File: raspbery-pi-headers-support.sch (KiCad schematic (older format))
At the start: 14 parts

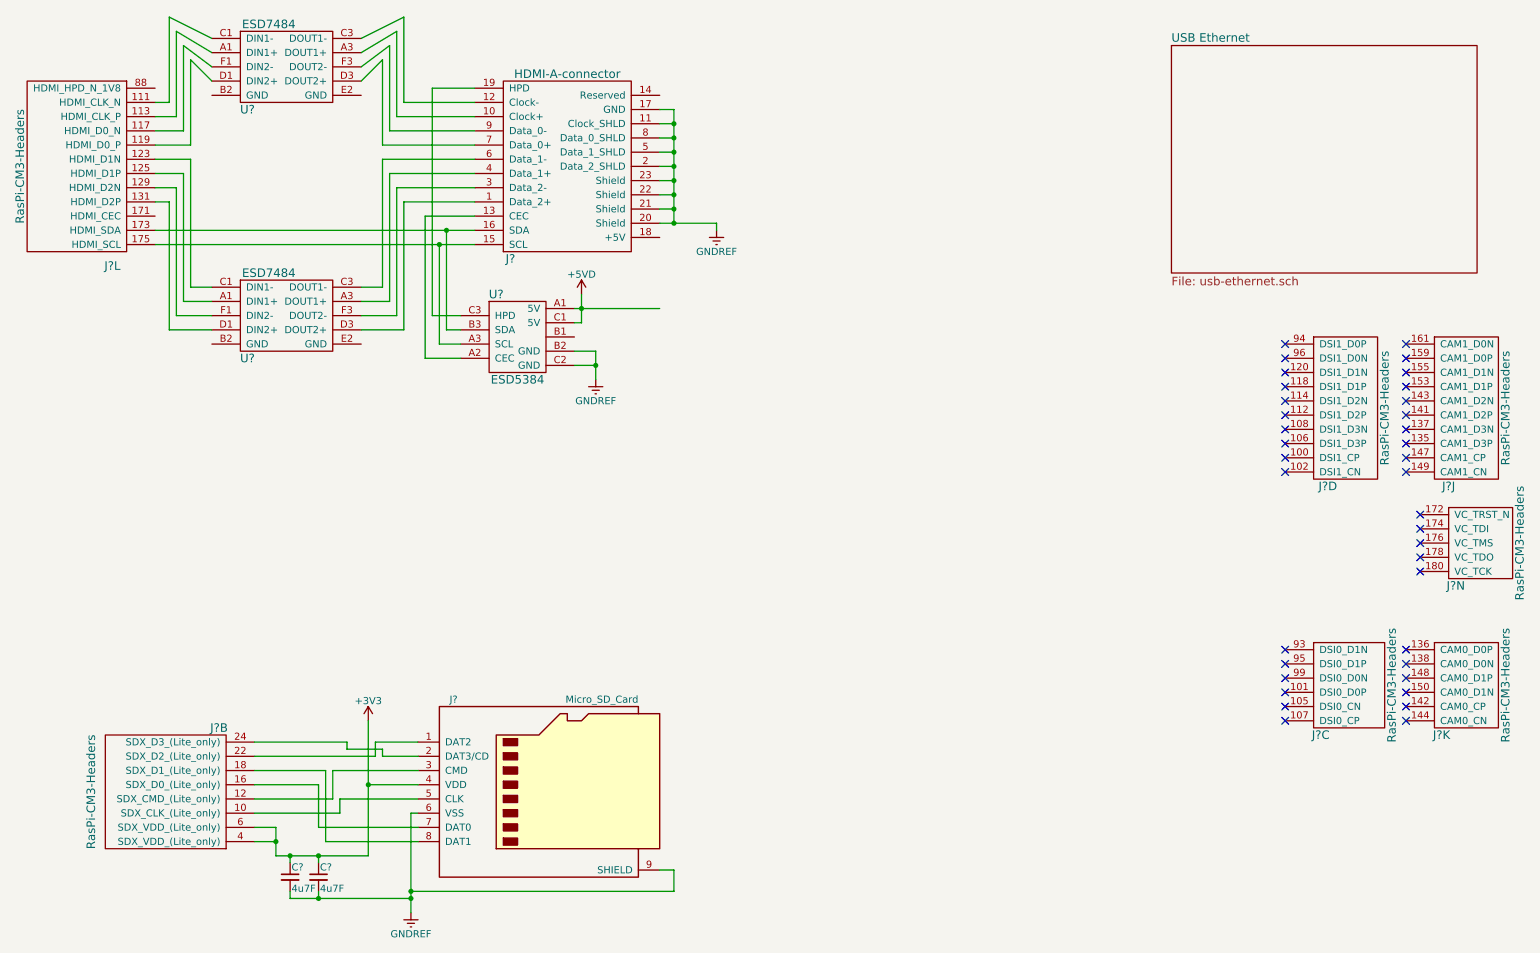
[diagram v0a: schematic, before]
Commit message: Worked on power for USB and finished ESD for hdmi
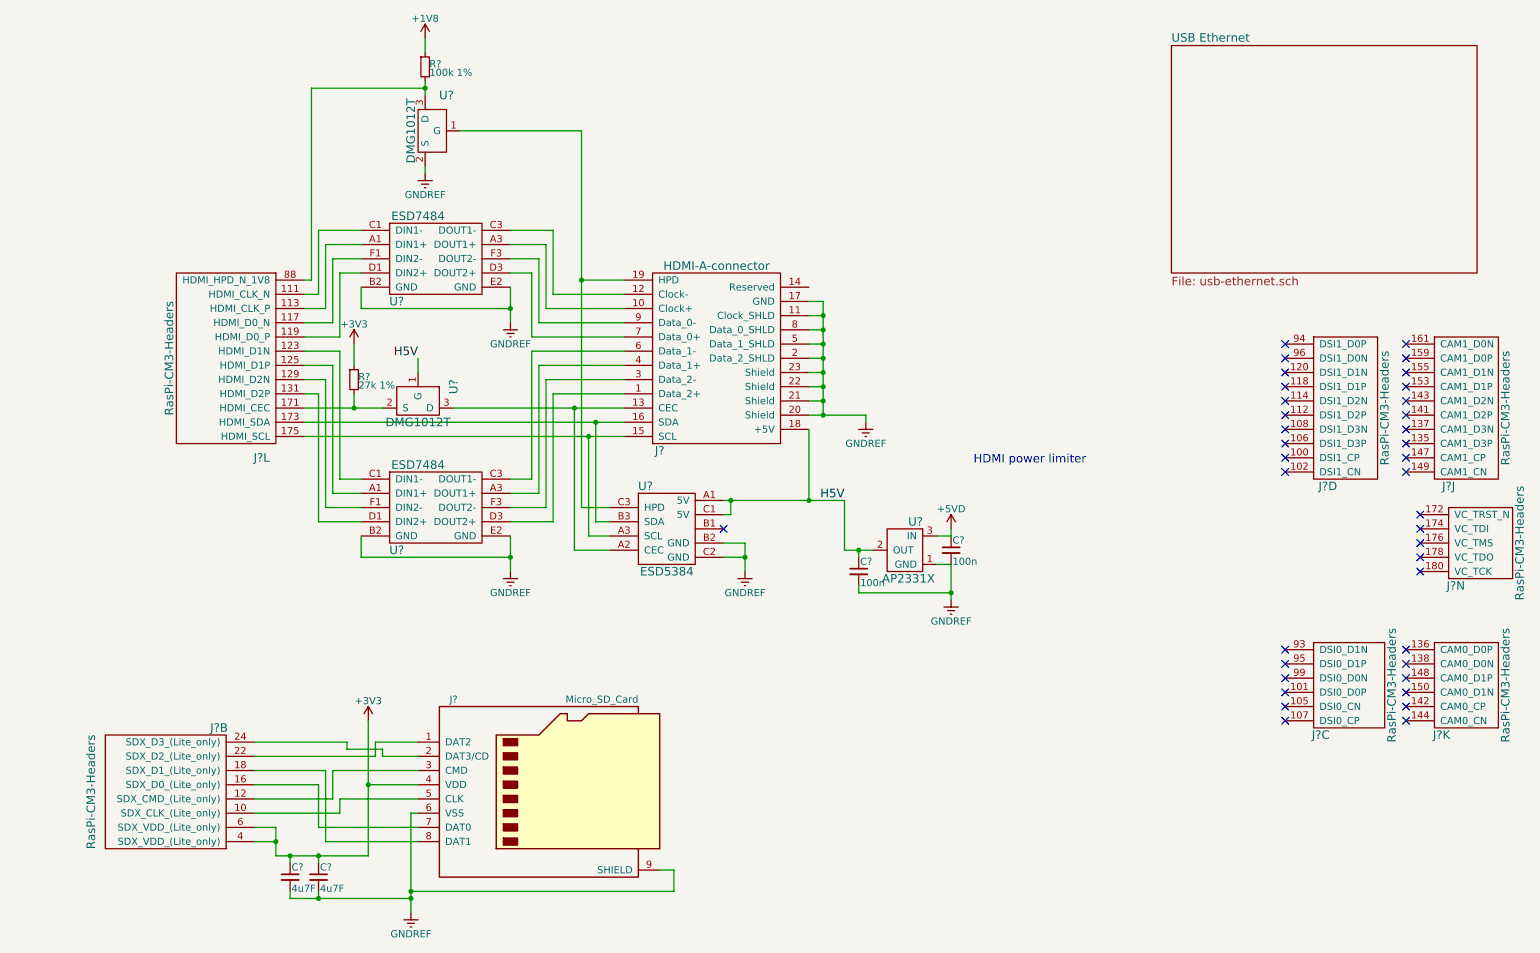
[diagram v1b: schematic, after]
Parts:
- added C? (x2): 100n, symbol C_Small
- added R?: 100k 1%, symbol R_Small
- added R?: 27k 1%, symbol R_Small
- added U? (x2): DMG1012T, symbol DMG1012T
- added U?: AP2331X, TO_SOT_Packages_SMD:SOT-23, symbol AP2331X
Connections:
- net +3V3: now also R?.1
- net +5VD: now also C?.1, U?.3 (IN); no longer U?.A1 (5V), U?.C1 (5V)
- net GNDREF: now also U?.B2 (GND), U?.B2 (GND), U?.E2 (GND), U?.E2 (GND), C?.2, C?.2, U?.1 (GND), U?.2 (S)
- net at J?.171 (HDMI_CEC): now also R?.2, U?.2 (S)
- net at J?.88 (HDMI_HPD_N_1V8): now also R?.2, U?.3 (D)
- net at J?.13 (CEC), U?.A2 (CEC): now also U?.3 (D)
- net H5V: now reaches J?.18 (+5V)
- net H5V: now also U?.A1 (5V), U?.C1 (5V), C?.1, U?.1 (G), U?.2 (OUT)
- net at J?.19 (HPD), U?.C3 (HPD): now also U?.1 (G)
- new net +1V8: R?.1
- no-connect marks 37 -> 38
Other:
- note added: "HDMI power limiter"
- moved on the sheet: J?, J?L, U?

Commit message: Started fixing DRC issues
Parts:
- C211, C212, C213, C214: renamed from C?; footprint (none) -> Capacitors_SMD:C_0603_HandSoldering
- R123, R124: renamed from R?; footprint (none) -> Capacitors_SMD:C_0603_HandSoldering
- gave numbers to parts that had none: 9
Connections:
- no-connect marks 38 -> 39
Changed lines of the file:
@@
 $EndDescr
 $Comp
-L RasPi-CM3-Headers J?
+L RasPi-CM3-Headers J1
 U 2 1 58ECDA7F
 P 1650 6000
-F 0 "J?" H 1350 5550 60  0000 C CNN
+F 0 "J1" H 1350 5550 60  0000 C CNN
 F 1 "RasPi-CM3-Headers" V 2250 6000 60  0000 C CNN
 F 2 "Sockets:Socket_SODIMM_DDR1-2_TE_1612618" H 1700 11100 60  0001 C CNN
@@
 $EndComp
 $Comp
-L RasPi-CM3-Headers J?
+L RasPi-CM3-Headers J1
 U 3 1 58ECDAC0
 P 9900 5250
-F 0 "J?" H 9700 4900 60  0000 C CNN
+F 0 "J1" H 9700 4900 60  0000 C CNN
 F 1 "RasPi-CM3-Headers" V 10200 5250 60  0000 C CNN
 F 2 "Sockets:Socket_SODIMM_DDR1-2_TE_1612618" H 9950 10350 60  0001 C CNN
@@
 $EndComp
 $Comp
-L RasPi-CM3-Headers J?
+L RasPi-CM3-Headers J1
 U 4 1 58ECDAF6
 P 9850 3300
-F 0 "J?" H 9750 2750 60  0000 C CNN
+F 0 "J1" H 9750 2750 60  0000 C CNN
 F 1 "RasPi-CM3-Headers" V 10150 3300 60  0000 C CNN
 F 2 "Sockets:Socket_SODIMM_DDR1-2_TE_1612618" H 9900 8400 60  0001 C CNN
@@
 $EndComp
 $Comp
-L RasPi-CM3-Headers J?
+L RasPi-CM3-Headers J1
 U 10 1 58ECDB2D
 P 10700 3300
-F 0 "J?" H 10600 2750 60  0000 C CNN
+F 0 "J1" H 10600 2750 60  0000 C CNN
 F 1 "RasPi-CM3-Headers" V 11000 3300 60  0000 C CNN
 F 2 "Sockets:Socket_SODIMM_DDR1-2_TE_1612618" H 10750 8400 60  0001 C CNN
@@
 $EndComp
 $Comp
-L RasPi-CM3-Headers J?
+L RasPi-CM3-Headers J1
 U 11 1 58ECDB78
 P 10700 5250
-F 0 "J?" H 10550 4900 60  0000 C CNN
+F 0 "J1" H 10550 4900 60  0000 C CNN
 F 1 "RasPi-CM3-Headers" V 11000 5250 60  0000 C CNN
 F 2 "Sockets:Socket_SODIMM_DDR1-2_TE_1612618" H 10750 10350 60  0001 C CNN
@@
 $EndComp
 $Comp
-L RasPi-CM3-Headers J?
+L RasPi-CM3-Headers J1
 U 12 1 58ECDBAE
 P 2100 2950
-F 0 "J?" H 1950 2250 60  0000 C CNN
+F 0 "J1" H 1950 2250 60  0000 C CNN
 F 1 "RasPi-CM3-Headers" V 2600 2950 60  0000 C CNN
 F 2 "Sockets:Socket_SODIMM_DDR1-2_TE_1612618" H 2150 8050 60  0001 C CNN
@@
 $EndComp
 $Comp
-L RasPi-CM3-Headers J?
+L RasPi-CM3-Headers J1
 U 14 1 58ECDBFE
 P 10700 4250
-F 0 "J?" H 10650 3950 60  0000 C CNN
+F 0 "J1" H 10650 3950 60  0000 C CNN
 F 1 "RasPi-CM3-Headers" V 11100 4250 60  0000 C CNN
 F 2 "Sockets:Socket_SODIMM_DDR1-2_TE_1612618" H 10750 9350 60  0001 C CNN
@@
 NoConn ~ 10400 4450
 $Comp
-L Micro_SD_Card J?
+L Micro_SD_Card J10
 U 1 1 591147C4
 P 4250 5950
-F 0 "J?" H 3600 6550 50  0000 C CNN
+F 0 "J10" H 3600 6550 50  0000 C CNN
 F 1 "Micro_SD_Card" H 4900 6550 50  0000 R CNN
 F 2 "" H 5400 6250 50  0001 C CNN
@@
 $EndComp
 $Comp
-L GNDREF #PWR?
+L GNDREF #PWR0152
 U 1 1 59114968
 P 3300 6850
-F 0 "#PWR?" H 3300 6600 50  0001 C CNN
+F 0 "#PWR0152" H 3300 6600 50  0001 C CNN
 F 1 "GNDREF" H 3300 6700 50  0000 C CNN
 F 2 "" H 3300 6850 50  0001 C CNN
@@
 $EndComp
 $Comp
-L +3V3 #PWR?
+L +3V3 #PWR0153
 U 1 1 59114A75
 P 3000 5500
-F 0 "#PWR?" H 3000 5350 50  0001 C CNN
+F 0 "#PWR0153" H 3000 5350 50  0001 C CNN
 F 1 "+3V3" H 3000 5640 50  0000 C CNN
 F 2 "" H 3000 5500 50  0001 C CNN
@@
 $EndComp
 $Comp
-L C_Small C?
+L C_Small C211
 U 1 1 5911519B
 P 2450 6600
-F 0 "C?" H 2460 6670 50  0000 L CNN
+F 0 "C211" H 2460 6670 50  0000 L CNN
 F 1 "4u7F" H 2460 6520 50  0000 L CNN
-F 2 "" H 2450 6600 50  0001 C CNN
+F 2 "Capacitors_SMD:C_0603_HandSoldering" H 2450 6600 50  0001 C CNN
 F 3 "" H 2450 6600 50  0001 C CNN
 	1    2450 6600
@@
 $EndComp
 $Comp
-L C_Small C?
+L C_Small C212
 U 1 1 5911521F
 P 2650 6600
-F 0 "C?" H 2660 6670 50  0000 L CNN
+F 0 "C212" H 2660 6670 50  0000 L CNN
 F 1 "4u7F" H 2660 6520 50  0000 L CNN
-F 2 "" H 2650 6600 50  0001 C CNN
+F 2 "Capacitors_SMD:C_0603_HandSoldering" H 2650 6600 50  0001 C CNN
 F 3 "" H 2650 6600 50  0001 C CNN
 	1    2650 6600
@@
 $EndComp
 $Comp
-L HDMI-A-connector J?
+L HDMI-A-connector J11
 U 1 1 5911658C
 P 5450 2950
-F 0 "J?" H 5050 3600 60  0000 C CNN
+F 0 "J11" H 5050 3600 60  0000 C CNN
 F 1 "HDMI-A-connector" H 5450 2300 60  0000 C CNN
 F 2 "" H 5450 2950 60  0001 C CNN
@@
 $EndComp
 $Comp
-L ESD5384 U?
+L ESD5384 U35
 U 1 1 591172E0
 P 5100 4150
-F 0 "U?" H 4950 4450 60  0000 C CNN
+F 0 "U35" H 4950 4450 60  0000 C CNN
 F 1 "ESD5384" H 5100 3850 60  0000 C CNN
 F 2 "" H 5100 4200 60  0001 C CNN
@@
 $EndComp
 $Comp
-L +5VD #PWR?
+L +5VD #PWR0154
 U 1 1 591176E4
 P 7100 4150
-F 0 "#PWR?" H 7100 4000 50  0001 C CNN
+F 0 "#PWR0154" H 7100 4000 50  0001 C CNN
 F 1 "+5VD" H 7100 4290 50  0000 C CNN
 F 2 "" H 7100 4150 50  0001 C CNN
@@
 Connection ~ 6200 2650
 $Comp
-L GNDREF #PWR?
+L GNDREF #PWR0155
 U 1 1 59117C76
 P 6500 3400
-F 0 "#PWR?" H 6500 3150 50  0001 C CNN
+F 0 "#PWR0155" H 6500 3150 50  0001 C CNN
 F 1 "GNDREF" H 6500 3250 50  0000 C CNN
 F 2 "" H 6500 3400 50  0001 C CNN
@@
 Connection ~ 6200 3350
 $Comp
-L GNDREF #PWR?
+L GNDREF #PWR0156
 U 1 1 59117D13
 P 5650 4450
-F 0 "#PWR?" H 5650 4200 50  0001 C CNN
+F 0 "#PWR0156" H 5650 4200 50  0001 C CNN
 F 1 "GNDREF" H 5650 4300 50  0000 C CNN
 F 2 "" H 5650 4450 50  0001 C CNN
@@
 Connection ~ 5650 4350
 $Comp
-L ESD7484 U?
+L ESD7484 U34
 U 1 1 5911871C
 P 3500 3950
-F 0 "U?" H 3200 3600 60  0000 C CNN
+F 0 "U34" H 3200 3600 60  0000 C CNN
 F 1 "ESD7484" H 3350 4200 60  0000 C CNN
 F 2 "" H 3500 3950 60  0001 C CNN
@@
 $EndComp
 $Comp
-L ESD7484 U?
+L ESD7484 U33
 U 1 1 591189BB
 P 3500 2200
-F 0 "U?" H 3200 1850 60  0000 C CNN
+F 0 "U33" H 3200 1850 60  0000 C CNN
 F 1 "ESD7484" H 3350 2450 60  0000 C CNN
 F 2 "" H 3500 2200 60  0001 C CNN
@@
 	4150 2350 4000 2350
 $Comp
-L DMG1012T U?
+L DMG1012T U31
 U 1 1 5911B6F8
 P 3150 1350
-F 0 "U?" H 2750 1600 60  0000 C CNN
+F 0 "U31" H 2750 1600 60  0000 C CNN
 F 1 "DMG1012T" V 3000 1350 60  0000 C CNN
 F 2 "" H 2750 1800 60  0001 C CNN
@@
 $EndComp
 $Comp
-L +1V8 #PWR?
+L +1V8 #PWR0157
 U 1 1 5911B770
 P 3400 700
-F 0 "#PWR?" H 3400 550 50  0001 C CNN
+F 0 "#PWR0157" H 3400 550 50  0001 C CNN
 F 1 "+1V8" H 3400 840 50  0000 C CNN
 F 2 "" H 3400 700 50  0001 C CNN
@@
 Connection ~ 4500 2400
 $Comp
-L R_Small R?
+L R_Small R124
 U 1 1 5911BA5B
 P 3400 900
-F 0 "R?" H 3430 920 50  0000 L CNN
+F 0 "R124" H 3430 920 50  0000 L CNN
 F 1 "100k 1%" H 3430 860 50  0000 L CNN
-F 2 "" H 3400 900 50  0001 C CNN
+F 2 "Capacitors_SMD:C_0603_HandSoldering" H 3400 900 50  0001 C CNN
 F 3 "" H 3400 900 50  0001 C CNN
 	1    3400 900
@@
 	3400 1000 3400 1100
 $Comp
-L GNDREF #PWR?
+L GNDREF #PWR0158
 U 1 1 5911BCE1
 P 3400 1650
-F 0 "#PWR?" H 3400 1400 50  0001 C CNN
+F 0 "#PWR0158" H 3400 1400 50  0001 C CNN
 F 1 "GNDREF" H 3400 1500 50  0000 C CNN
 F 2 "" H 3400 1650 50  0001 C CNN
@@
 Connection ~ 3400 1050
 $Comp
-L AP2331X U?
+L AP2331X U36
 U 1 1 5911C05E
 P 6700 4150
-F 0 "U?" H 6550 4200 60  0000 C CNN
+F 0 "U36" H 6550 4200 60  0000 C CNN
 F 1 "AP2331X" H 6600 3800 60  0000 C CNN
 F 2 "TO_SOT_Packages_SMD:SOT-23" H 6800 5100 60  0001 C CNN
@@
 	6100 3950 6100 3450
 $Comp
-L C_Small C?
+L C_Small C214
 U 1 1 5911FC51
 P 7100 4300
-F 0 "C?" H 7110 4370 50  0000 L CNN
+F 0 "C214" H 7110 4370 50  0000 L CNN
 F 1 "100n" H 7110 4220 50  0000 L CNN
-F 2 "" H 7100 4300 50  0001 C CNN
+F 2 "Capacitors_SMD:C_0603_HandSoldering" H 7100 4300 50  0001 C CNN
 F 3 "" H 7100 4300 50  0001 C CNN
 	1    7100 4300
@@
 	7000 4400 7100 4400
 $Comp
-L GNDREF #PWR?
+L GNDREF #PWR0159
 U 1 1 5911FE33
 P 7100 4650
-F 0 "#PWR?" H 7100 4400 50  0001 C CNN
+F 0 "#PWR0159" H 7100 4400 50  0001 C CNN
 F 1 "GNDREF" H 7100 4500 50  0000 C CNN
 F 2 "" H 7100 4650 50  0001 C CNN
@@
 	5550 4050 5550 3950
 $Comp
-L C_Small C?
+L C_Small C213
 U 1 1 59120198
 P 6450 4450
-F 0 "C?" H 6460 4520 50  0000 L CNN
+F 0 "C213" H 6460 4520 50  0000 L CNN
 F 1 "100n" H 6460 4370 50  0000 L CNN
-F 2 "" H 6450 4450 50  0001 C CNN
+F 2 "Capacitors_SMD:C_0603_HandSoldering" H 6450 4450 50  0001 C CNN
 F 3 "" H 6450 4450 50  0001 C CNN
 	1    6450 4450
@@
 H5V
 $Comp
-L GNDREF #PWR?
+L GNDREF #PWR0160
 U 1 1 5912041E
 P 4000 4450
-F 0 "#PWR?" H 4000 4200 50  0001 C CNN
+F 0 "#PWR0160" H 4000 4200 50  0001 C CNN
 F 1 "GNDREF" H 4000 4300 50  0000 C CNN
 F 2 "" H 4000 4450 50  0001 C CNN
@@
 NoConn ~ 5500 4150
 $Comp
-L GNDREF #PWR?
+L GNDREF #PWR0161
 U 1 1 59120752
 P 4000 2700
-F 0 "#PWR?" H 4000 2450 50  0001 C CNN
+F 0 "#PWR0161" H 4000 2450 50  0001 C CNN
 F 1 "GNDREF" H 4000 2550 50  0000 C CNN
 F 2 "" H 4000 2700 50  0001 C CNN
@@
 Connection ~ 4000 2600
 $Comp
-L DMG1012T U?
+L DMG1012T U32
 U 1 1 591207FB
 P 3350 3550
-F 0 "U?" H 2950 3800 60  0000 C CNN
+F 0 "U32" H 2950 3800 60  0000 C CNN
 F 1 "DMG1012T" V 3200 3550 60  0000 C CNN
 F 2 "" H 2950 4000 60  0001 C CNN
@@
 Connection ~ 4450 3300
 $Comp
-L R_Small R?
+L R_Small R123
 U 1 1 591214D4
 P 2900 3100
-F 0 "R?" H 2930 3120 50  0000 L CNN
+F 0 "R123" H 2930 3120 50  0000 L CNN
 F 1 "27k 1%" H 2930 3060 50  0000 L CNN
-F 2 "" H 2900 3100 50  0001 C CNN
+F 2 "Capacitors_SMD:C_0603_HandSoldering" H 2900 3100 50  0001 C CNN
 F 3 "" H 2900 3100 50  0001 C CNN
 	1    2900 3100
@@
 Connection ~ 2900 3300
 $Comp
-L +3V3 #PWR?
+L +3V3 #PWR0162
 U 1 1 59121601
 P 2900 2850
-F 0 "#PWR?" H 2900 2700 50  0001 C CNN
+F 0 "#PWR0162" H 2900 2700 50  0001 C CNN
 F 1 "+3V3" H 2900 2990 50  0000 C CNN
 F 2 "" H 2900 2850 50  0001 C CNN
@@
 Wire Wire Line
 	2900 2850 2900 3000
+NoConn ~ 6100 2450
 $EndSCHEMATC
